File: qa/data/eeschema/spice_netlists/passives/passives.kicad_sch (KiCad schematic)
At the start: 4 parts

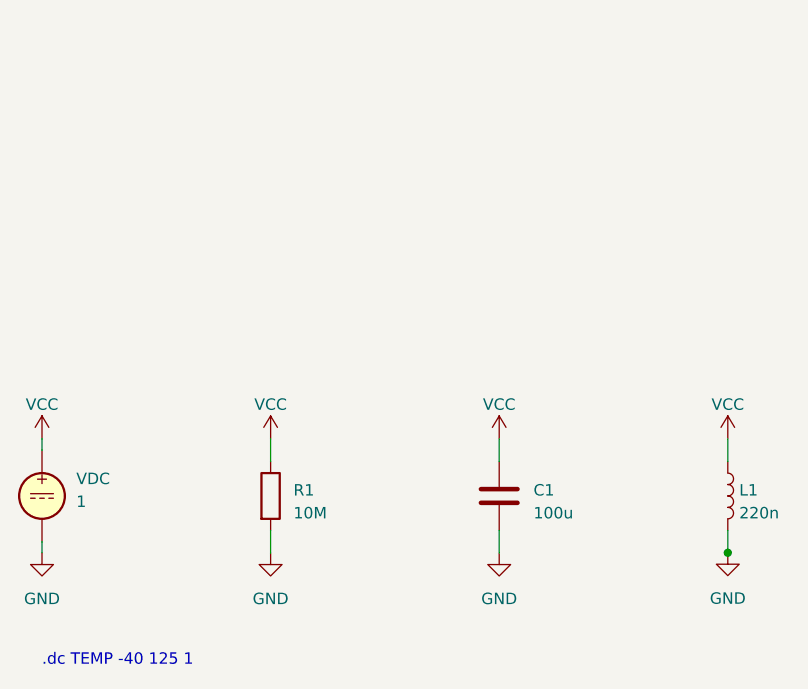
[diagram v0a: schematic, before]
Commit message: Spice transmission line models
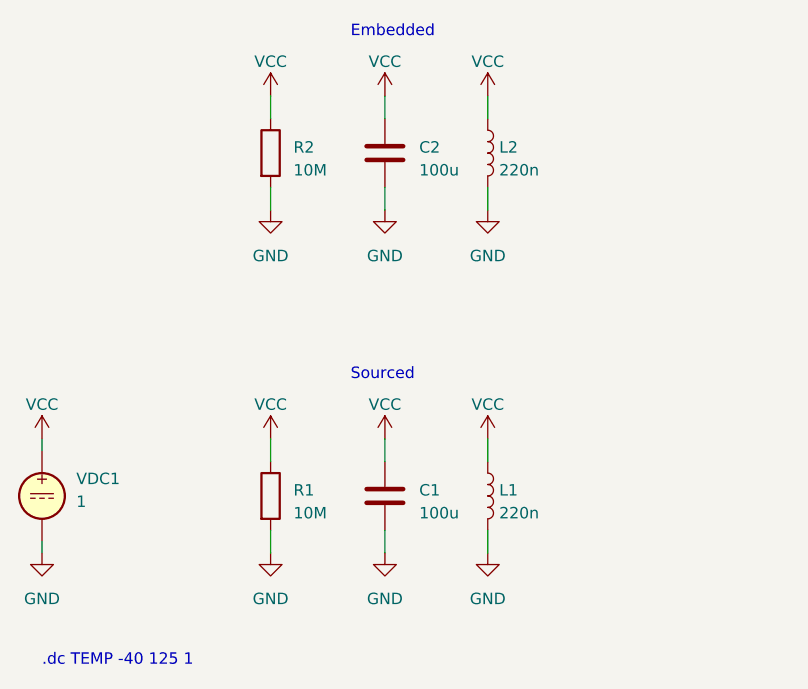
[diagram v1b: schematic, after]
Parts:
- added C2: 100u, symbol Device:C
- added L2: 220n, symbol Device:L
- added R2: 10M, symbol Device:R
- R1: Model_Pins (none) -> 1 2
- renumbered VDC to VDC1
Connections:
- net GND: now also C2.2, L2.2, R2.2
- net VCC: now also C2.1, L2.1, R2.1
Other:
- note added: "Embedded"
- note added: "Sourced"
- moved on the sheet: C1, L1
